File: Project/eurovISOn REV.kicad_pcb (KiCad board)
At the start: 2 copper layers, 266.7 x 85.7 mm, 160 parts, among them IC1 W25Q16JVUXIQ, J2 JST SH, J3 Pico EZmate, J5 TC2030_SWD, SW1 boot, SW2 SW_Push, SW3 RotaryEncoder_Switch, SW4 RotaryEncoder_Switch, SW5 RotaryEncoder_Switch, SW6 RotaryEncoder_Switch, U1 74AHCT1G125, U3 RP2040, U4 XC6206PxxxMR-Regulator_Linear, Y1 12MHz

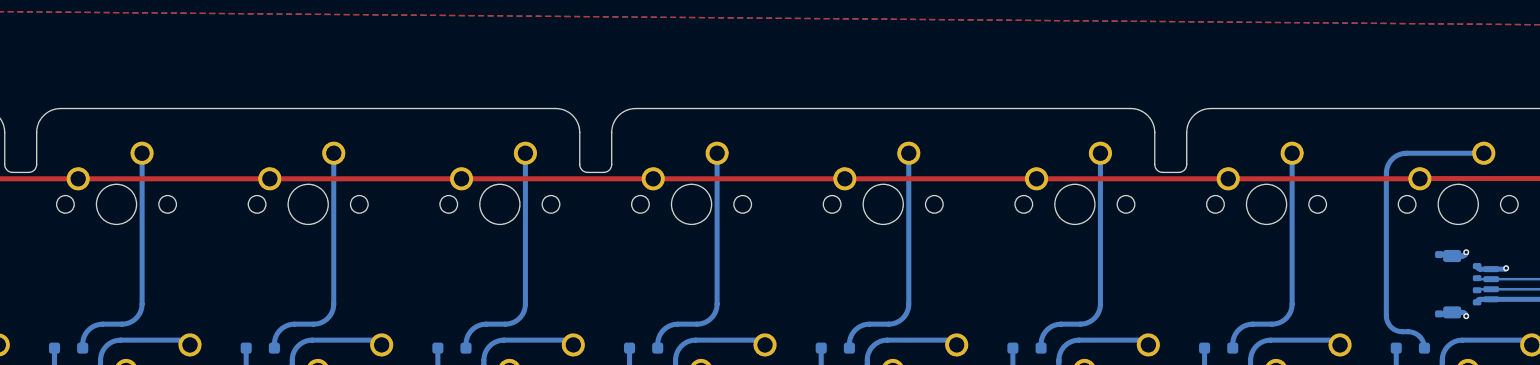
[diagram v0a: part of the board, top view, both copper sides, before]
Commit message: rev wip
usb port added
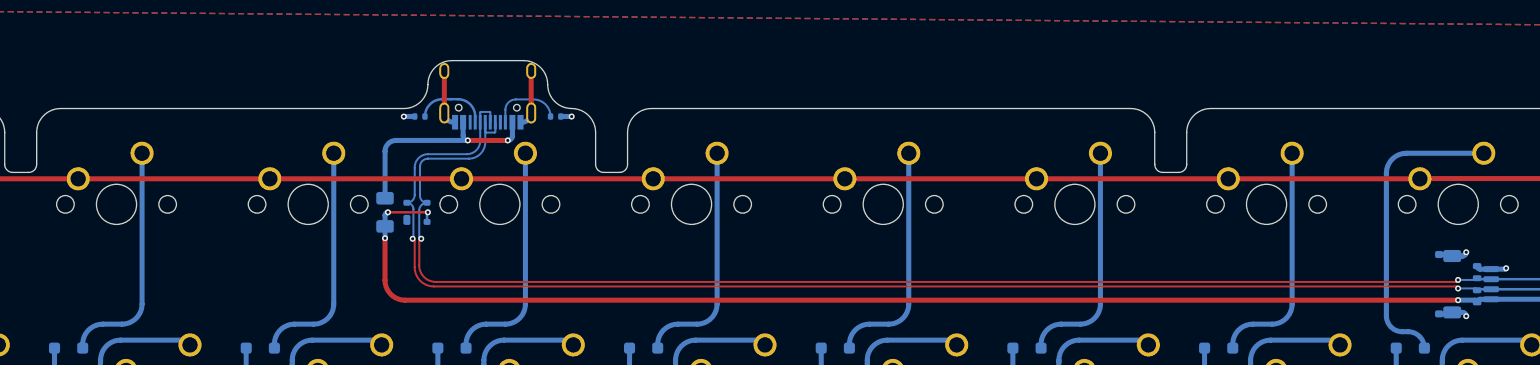
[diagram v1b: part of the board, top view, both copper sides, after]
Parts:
- added F1: 500mA, Fuse:Fuse_1206_3216Metric, B.Cu at (129.9, 32.5)
- added J1: USB_C_Receptacle_USB2.0, Connector_USB:USB_C_Receptacle_HRO_TYPE-C-31-M-12, B.Cu at (140.1, 19.5)
- added R2: 5k1, Resistor_SMD:R_0402_1005Metric, B.Cu at (133.3, 23.0)
- added R3: 5k1, Resistor_SMD:R_0402_1005Metric, B.Cu at (146.8, 23.0)
- added U5: PRTR5V0U2X, Package_TO_SOT_SMD:SOT-143, B.Cu at (133.0, 32.5)
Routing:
- net D_N: track 58.1 -> 188.5 mm, vias 1 -> 3
- net D_P: track 59.6 -> 189.4 mm, vias 1 -> 3
- net +5V: track 229.1 -> 350.7 mm, vias 19 -> 23
- net VBUS: track 0.00 -> 21.5 mm, vias 0 -> 2
- net GND: track 121.1 -> 134.7 mm, vias 42 -> 44
- net /CC1: track 0.00 -> 7.39 mm
- net /CC2: track 0.00 -> 7.17 mm
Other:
- outline, holes or cut-outs redrawn
- board text added: "JLCJLCJLCJLC"

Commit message: wip
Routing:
- net ROW2: track 297.8 -> 297.1 mm
- net +5V: track 350.7 -> 350.1 mm

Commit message: readme update
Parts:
- turned C16 to 0 degrees
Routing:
- net GND: track 134.7 -> 136.2 mm, vias 44 -> 45
- net +5V: track 350.1 -> 351.1 mm
